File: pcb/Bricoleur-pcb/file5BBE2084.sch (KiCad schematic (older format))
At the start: 27 parts, among them J2 Conn_02x10_Odd_Even, SW3 SW_Push, SW4 SW_Push, SW5 SW_Push

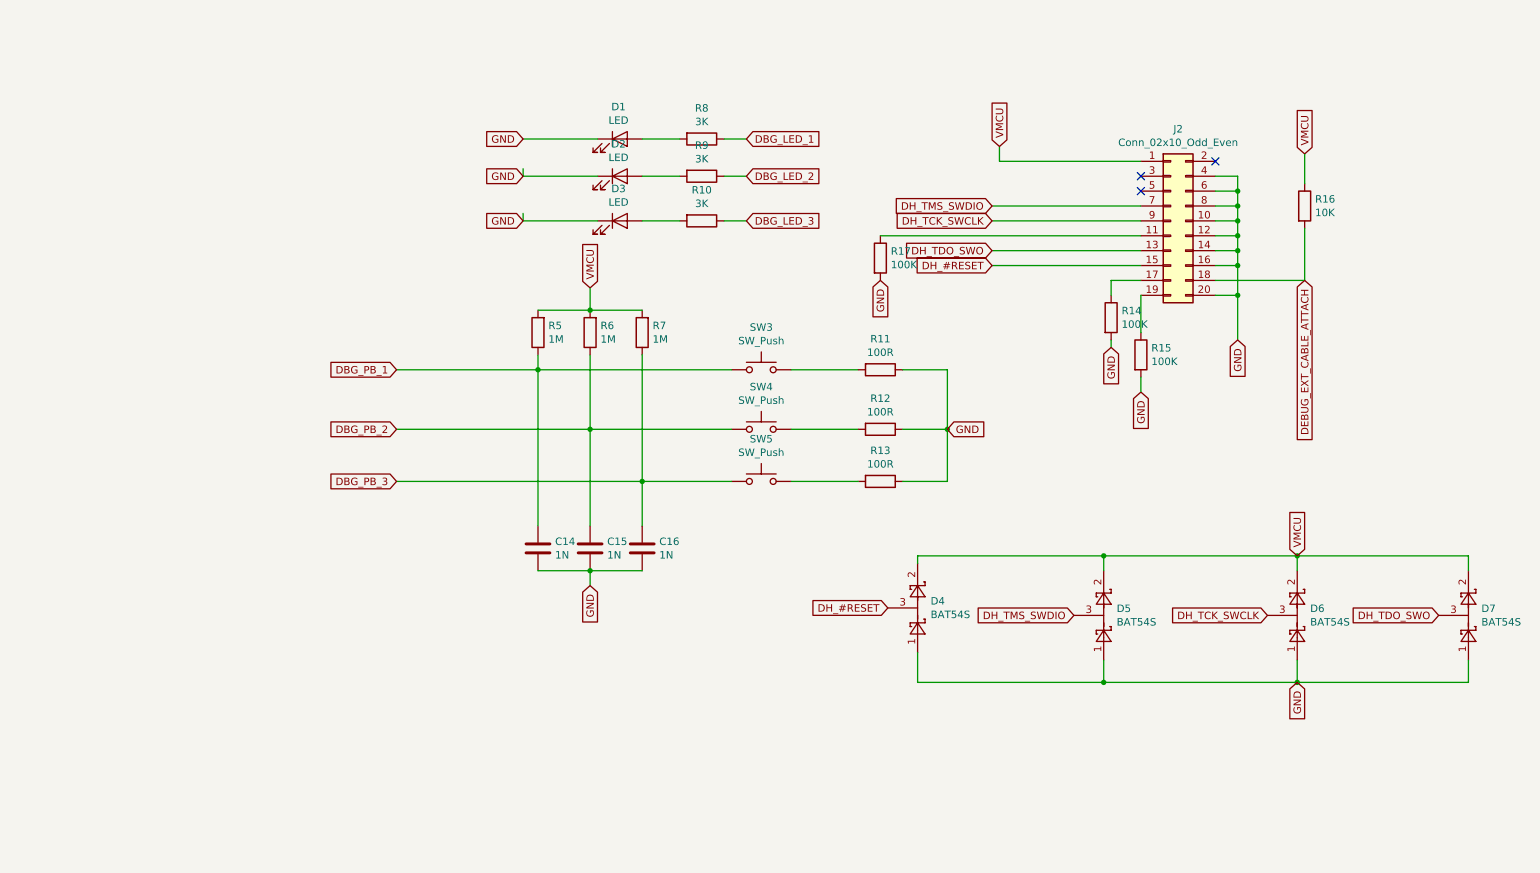
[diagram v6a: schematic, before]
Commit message: Cleanup, labeling, schematic size reduction
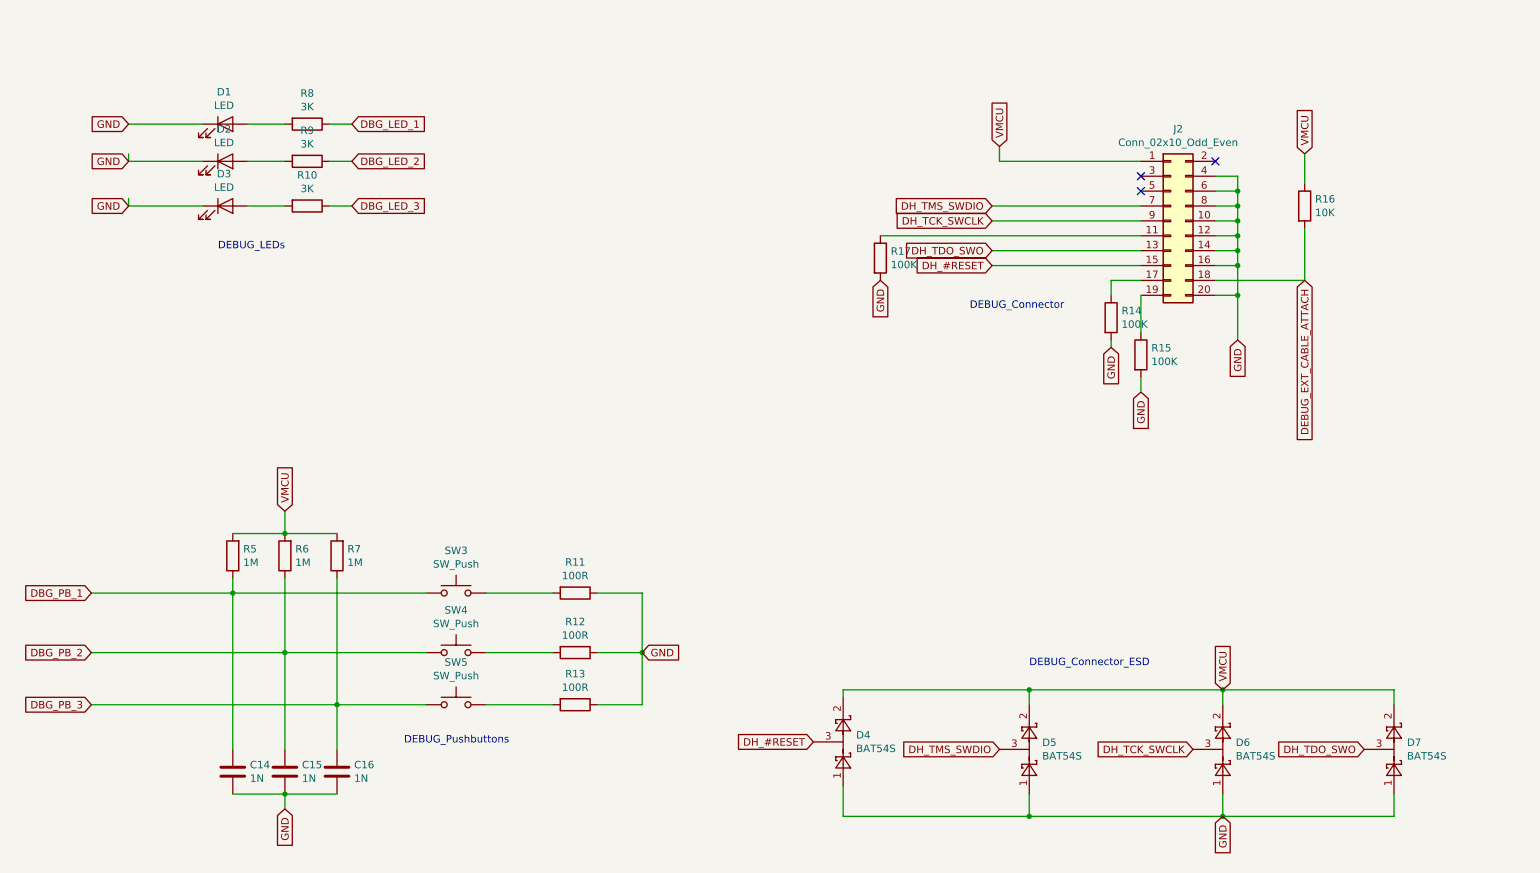
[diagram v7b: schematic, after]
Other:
- note added: "DEBUG_Connector"
- note added: "DEBUG_Connector_ESD\n"
- note added: "DEBUG_LEDs\n"
- note added: "DEBUG_Pushbuttons\n\n"
- moved on the sheet: C14, C15, C16, D1, D2, D3, D4, D5, D6, D7, R10, R11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
